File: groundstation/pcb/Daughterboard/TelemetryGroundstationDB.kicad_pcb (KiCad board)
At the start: 2 copper layers, 40 x 70 mm, 32 parts, among them J1 RFPC-SMA27-F, J2 ICD15S13E4GV00LF, M1 M4 Mounting Hole, M2 M4 Mounting Hole, M3 M4 Mounting Hole, M4 M4 Mounting Hole, U1 RC1780HP-RC232

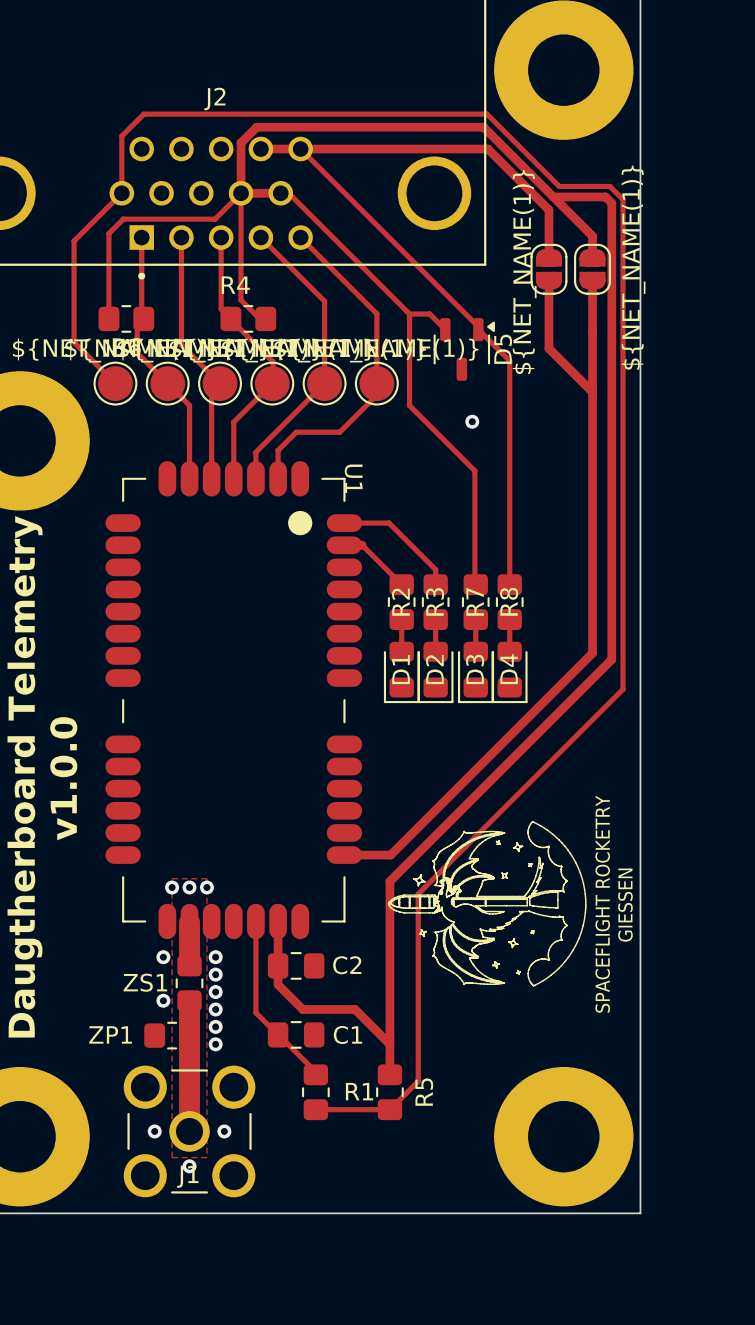
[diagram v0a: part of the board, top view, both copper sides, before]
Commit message: add silkscreen do daughterbaord
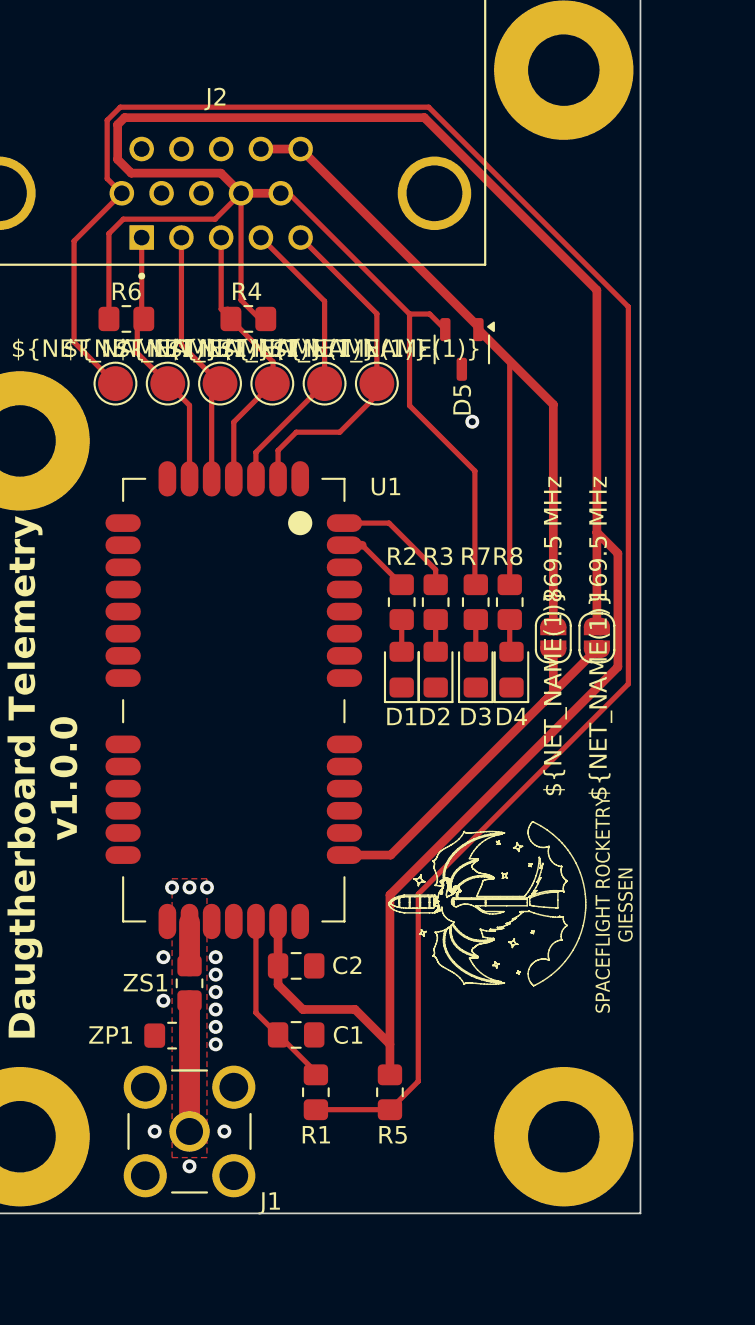
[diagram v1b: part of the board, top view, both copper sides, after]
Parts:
- moved JP1 21.2 mm to (15.0, 7.07)
- moved JP2 21.2 mm to (17.5, 7.07)
- moved D4 0.10 mm to (12.6, 8.88)
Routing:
- net Net-(JP1-B): track 49.0 -> 23.7 mm
- net +3V3: track 153.1 -> 165.4 mm
- net RST: track 109.6 -> 108.5 mm
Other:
- board text added: "169.5 MHz"
- board text added: "869.5 MHz"

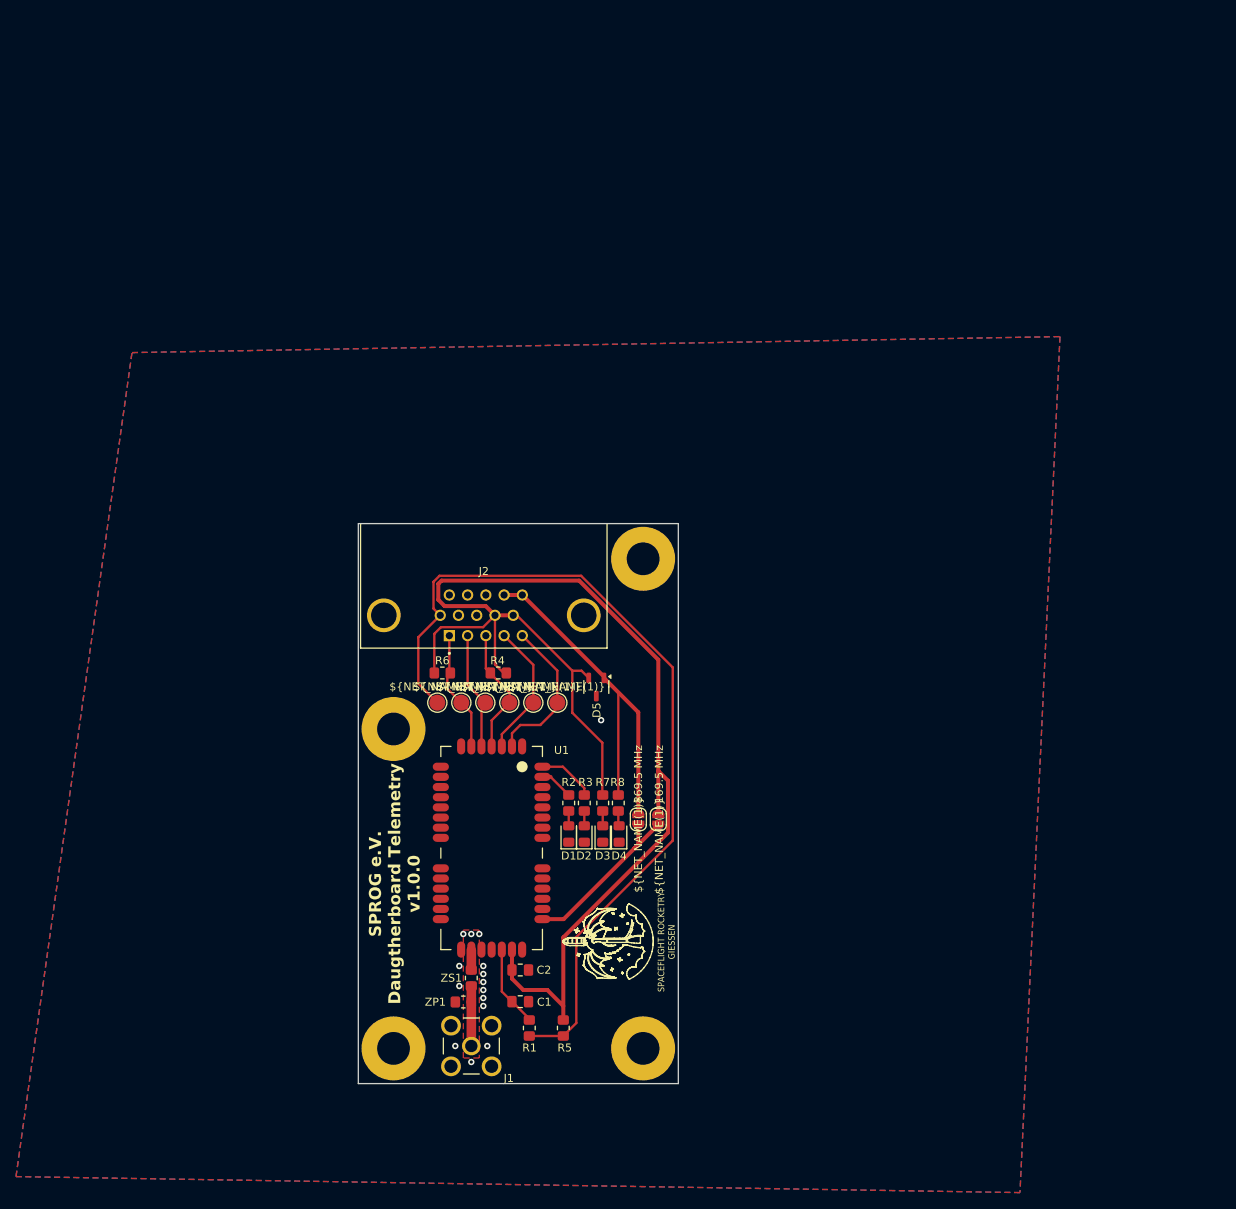
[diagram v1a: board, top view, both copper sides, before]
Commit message: improve DB silkscreen and edge cuts
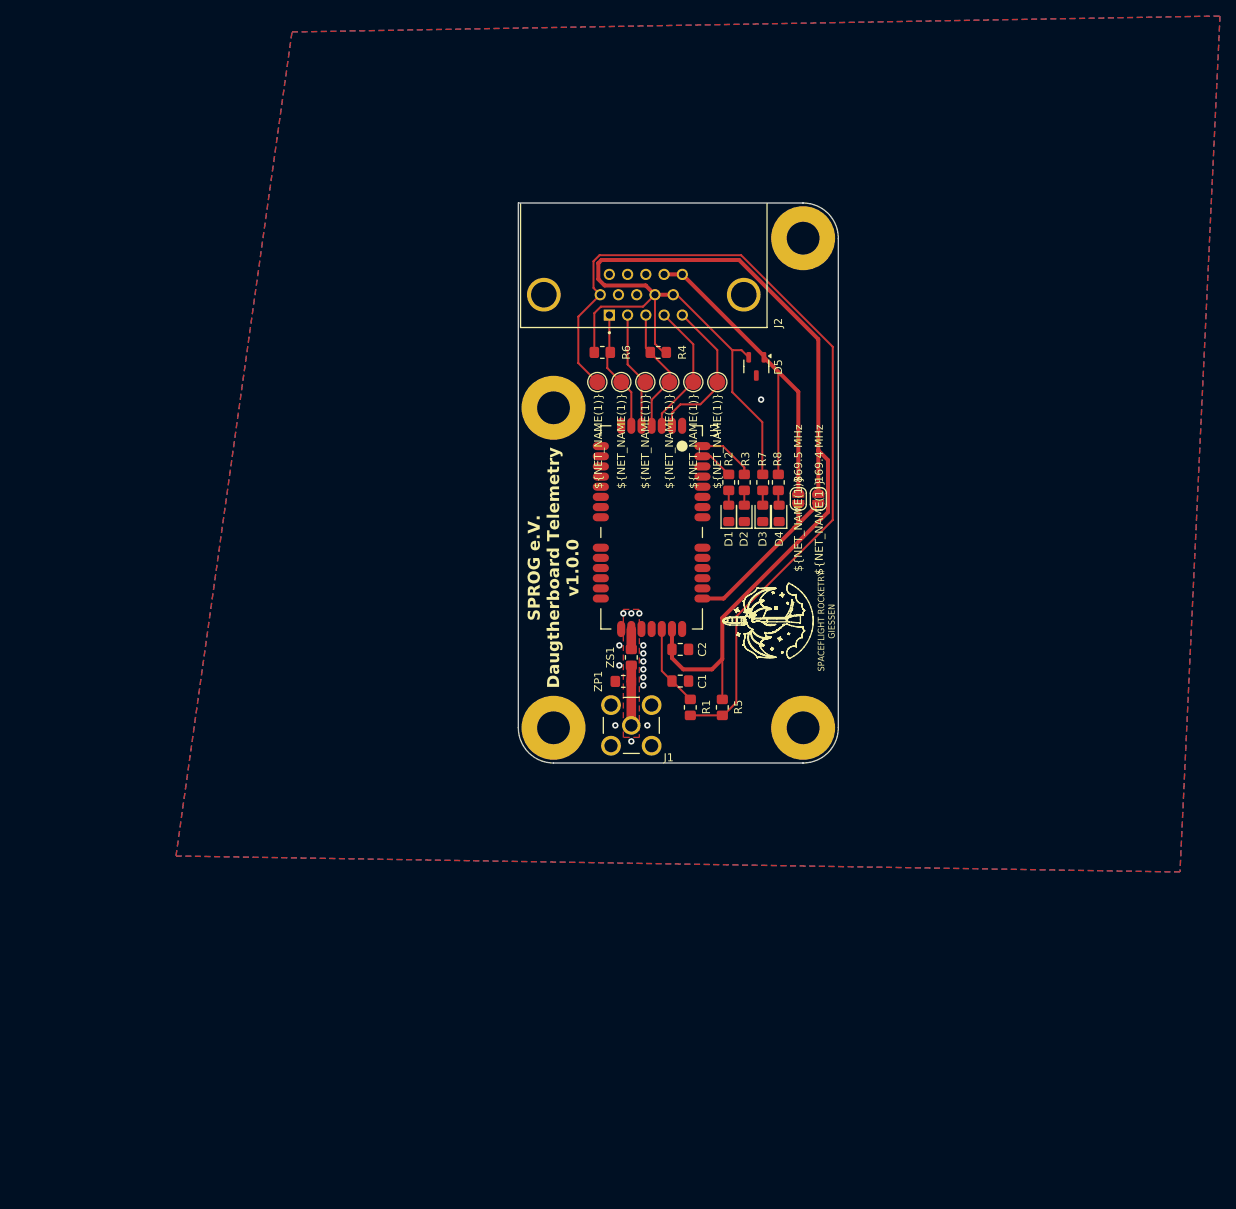
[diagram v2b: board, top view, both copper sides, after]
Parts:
- moved M3 44.9 mm to (4.40, -44.4)
- moved R1 44.8 mm to (21.5, -6.95)
- moved C1 44.8 mm to (20.2, -10.2)
- moved C2 44.8 mm to (20.2, -14.2)
- moved D1 44.8 mm to (26.3, -31.2)
- moved D2 44.8 mm to (28.2, -31.2)
- moved D3 44.8 mm to (30.6, -31.2)
- moved D4 44.8 mm to (32.6, -31.2)
- moved D5 44.8 mm to (29.8, -49.6)
- moved J1 44.8 mm to (14.1, -4.70)
- moved R2 44.8 mm to (26.3, -35.1)
- moved R3 44.8 mm to (28.2, -35.1)
- moved R4 44.8 mm to (17.5, -51.3)
- moved R6 44.8 mm to (10.5, -51.3)
- moved R7 44.8 mm to (30.6, -35.1)
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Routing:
- net +3V3: track 165.4 -> 163.3 mm
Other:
- outline, holes or cut-outs redrawn
- board text added: "169.4 MHz"
- board text removed: "169.5 MHz"
